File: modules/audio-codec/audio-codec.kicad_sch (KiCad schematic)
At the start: 24 parts, among them U1 TLV320AIC3110IRHBR, U2 ADP5301ACBZ-1-R7

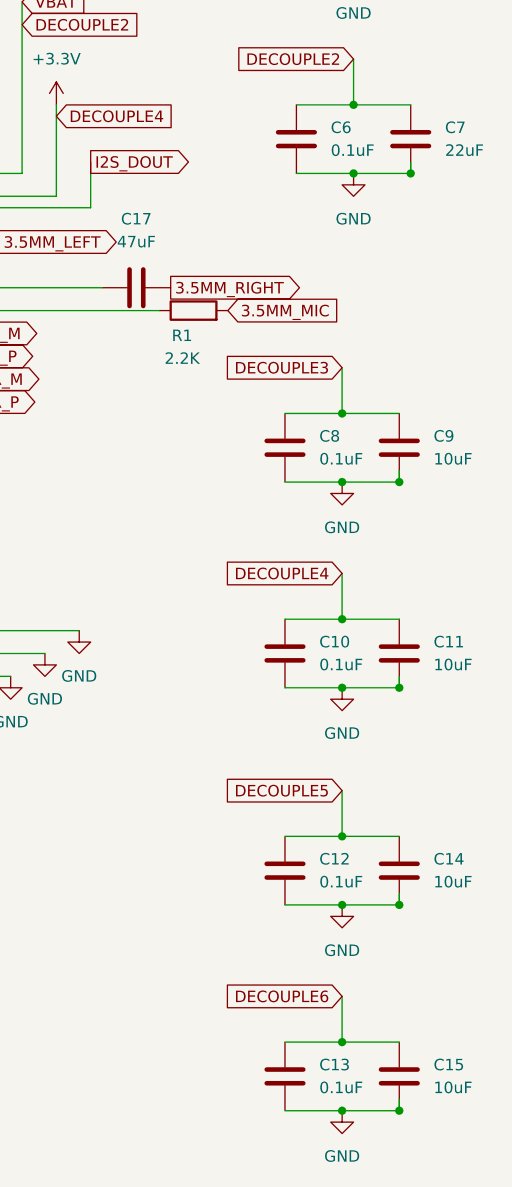
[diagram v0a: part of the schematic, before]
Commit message: Adding Mouser parts to sc
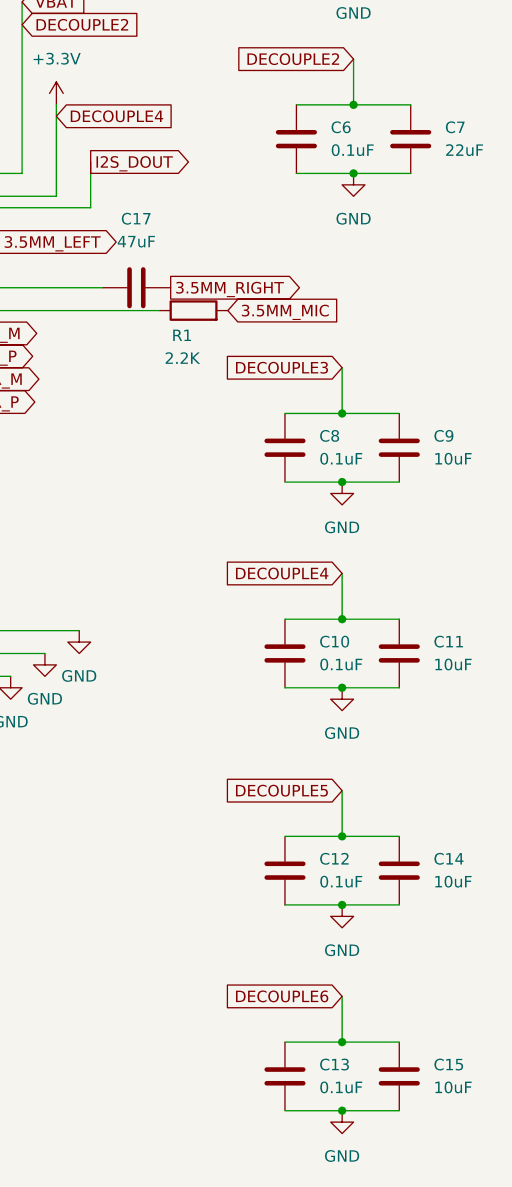
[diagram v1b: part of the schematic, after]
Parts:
- C1, C10, C12, C13, C4, C6, C8: Mfr. PN (none) -> C0603C104M4RAC; Mouser (none) -> https://hr.mouser.com/ProductDetail/KEMET/C0603C104M4RAC?qs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; Mouser PN (none) -> 80-C0603C104M4RAC
- C11, C14, C15, C2, C3, C9: Mfr. PN (none) -> C0603C106M9PAC7411; Mouser (none) -> https://hr.mouser.com/ProductDetail/KEMET/C0603C106M9PAC741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; Mouser PN (none) -> 80-C0603C106M9P7411
- C16, C17: Mfr. PN (none) -> GRM188R60E476ME15J; Mouser (none) -> https://hr.mouser.com/ProductDetail/Murata-Electronics/GRM1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; Mouser PN (none) -> 81-GRM188R60E476ME5J
- C5, C7: Mfr. PN (none) -> CC0603MRX5R5BB226; Mouser (none) -> https://hr.mouser.com/ProductDetail/YAGEO/CC0603MRX5R5BB226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; Mouser PN (none) -> 603-CC603MRX5R5BB226
- L1: Mfr. PN (none) -> MLP2016V2R2MT0S1; Mouser (none) -> https://hr.mouser.com/ProductDetail/TDK/MLP2016V2R2MT0S1?qs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; Mouser PN (none) -> 810-MLP2016V2R2MT0S1
- R1: Mfr. PN (none) -> RT0603DRE072K2L; Mouser (none) -> https://hr.mouser.com/ProductDetail/YAGEO/RT0603DRE072K2L?q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; Mouser PN (none) -> 603-RT0603DRE072K2L
- R2: Mfr. PN (none) -> RT0603BRD0719K6L; Mouser (none) -> https://hr.mouser.com/ProductDetail/YAGEO/RT0603BRD0719K6L?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; Mouser PN (none) -> 603-RT0603BRD0719K6L
- R3: Mfr. PN (none) -> RC0603FR-07100KL; Mouser (none) -> https://hr.mouser.com/ProductDetail/YAGEO/RC0603FR-07100KL?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; Mouser PN (none) -> 603-RC0603FR-07100KL
- U1: Mfr. PN (none) -> TLV320AIC3110IRHBR; Mouser (none) -> https://hr.mouser.com/ProductDetail/Texas-Instruments/TLV32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; Mouser PN (none) -> 595-V320AIC3110IRHBR
- U2: Mfr. PN (none) -> ADP5301ACBZ-1-R7; Mouser (none) -> https://hr.mouser.com/ProductDetail/Analog-Devices/ADP5301A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; Mouser PN (none) -> 584-ADP5301ACBZ-1-R7
